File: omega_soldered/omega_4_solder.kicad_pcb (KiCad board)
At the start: 2 copper layers, 204.8 x 78 mm, 83 parts, among them J1 Conn_01x02_Female, U1 ProMicro

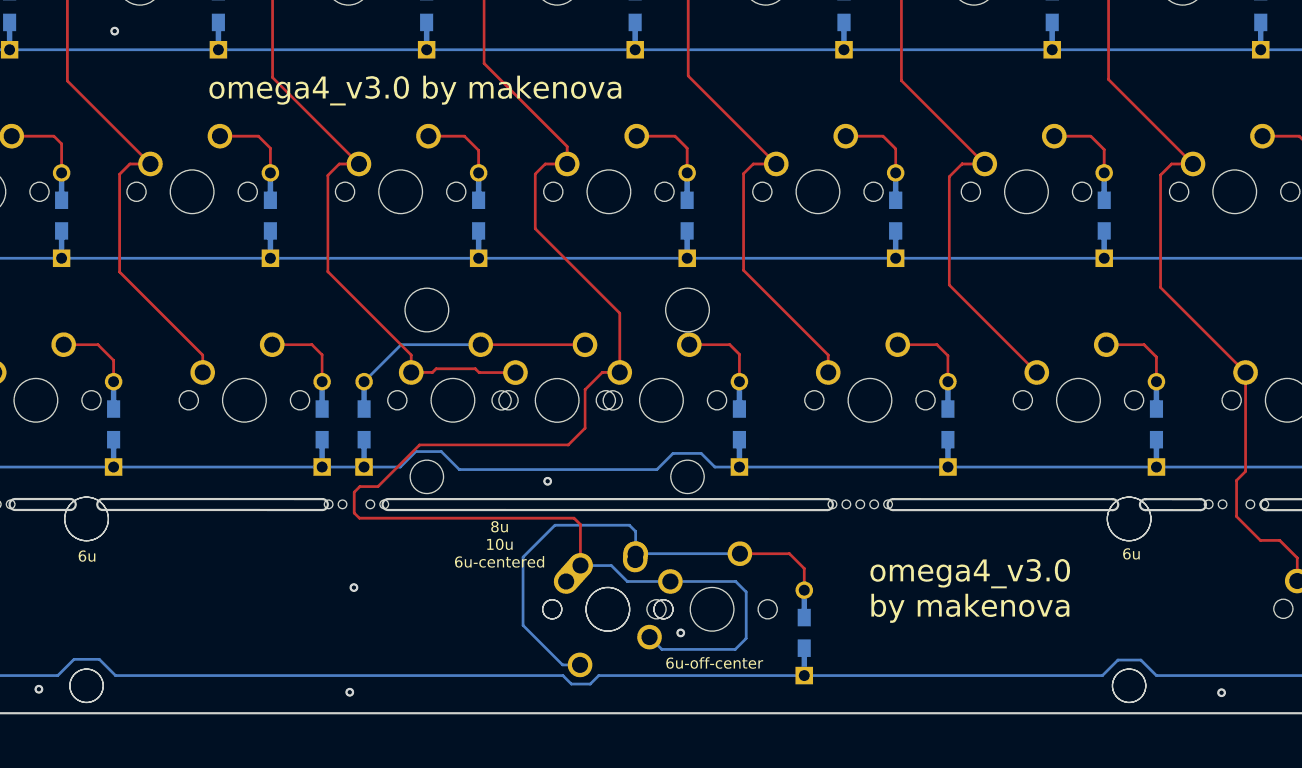
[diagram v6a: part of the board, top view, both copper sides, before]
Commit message: add split spacebar to breakaway row
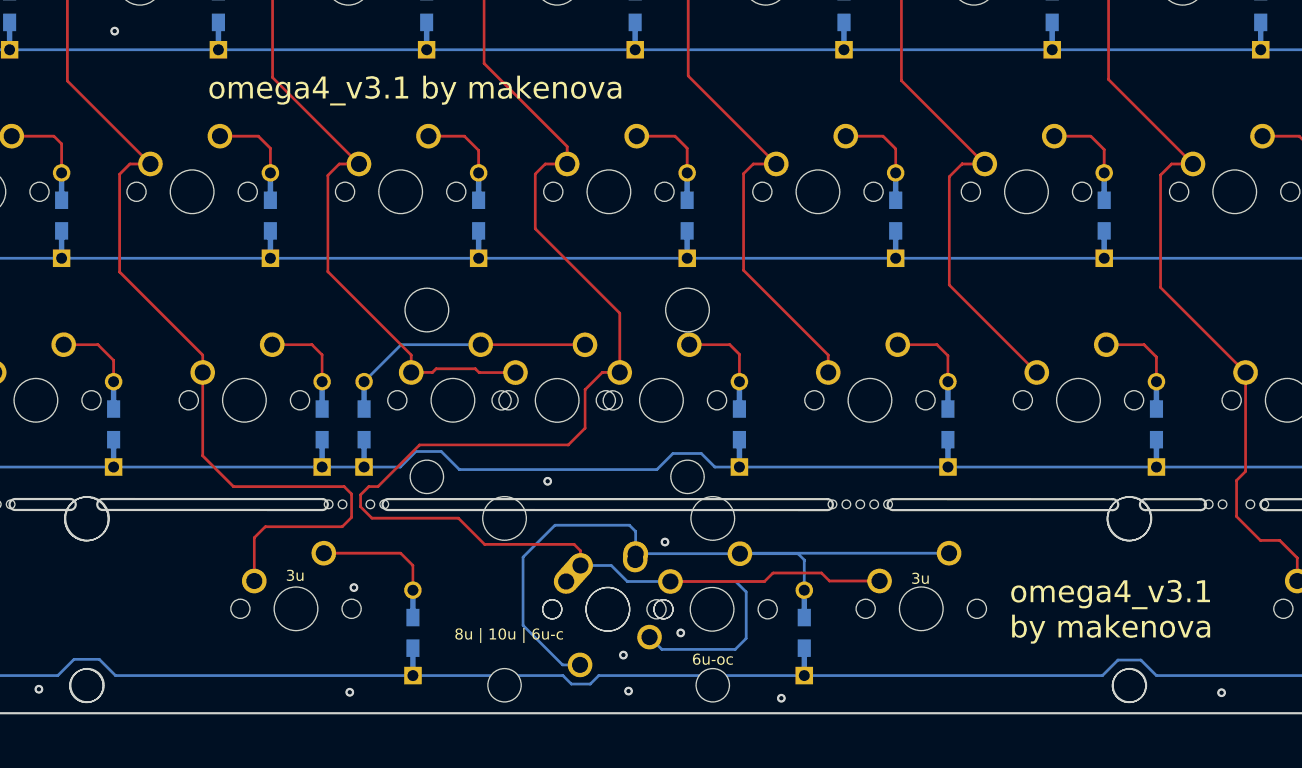
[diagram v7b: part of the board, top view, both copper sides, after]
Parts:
- added D36: D_Small, Keebio-Parts:Diode-Hybrid-Back, F.Cu at (140.4, 124.9)
- added MX39: MX-NoLED, MX_Only:MXOnly-3U-ReversedStabilizers-NoLED, F.Cu at (129.7, 122.7)
- added MX40: MX-NoLED, MX_Only:MXOnly-3U-ReversedStabilizers-NoLED, F.Cu at (186.8, 122.7)
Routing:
- net COL3: track 99.4 -> 137.8 mm
- net Net-(D33-Pad2): track 44.9 -> 64.6 mm
- net COL5: track 208.4 -> 225.1 mm
- net Net-(D36-Pad2): track 0.00 -> 10.9 mm
- net GND: vias 18 -> 22
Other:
- board text added: "3u"
- board text added: "6u-oc"
- board text added: "8u | 10u | 6u-c"
- board text added: "omega4_v3.1 by makenova"
- board text removed: "6u"
- board text removed: "6u-off-center"
- board text removed: "8u 10u 6u-centered"
- board text removed: "omega4_v3.0 by makenova"

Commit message: update readme images
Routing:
- net ROW3: track 237.6 -> 240.1 mm
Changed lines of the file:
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@@
   (segment (start 76.577741 109.802259) (end 76.577741 113.656741) (width 0.25) (layer "F.Cu") (net 34))
   (segment (start 75.20074 82.51285) (end 75.20074 95.26674) (width 0.25) (layer "F.Cu") (net 34))
-  (segment (start 111.716 127.3175) (end 113.1985 128.8) (width 0.25) (layer "B.Cu") (net 34))
+  (segment (start 226.025 127.5) (end 223.7185 127.5) (width 0.25) (layer "B.Cu") (net 34))
   (segment (start 93.025 127.45) (end 94.375 128.8) (width 0.25) (layer "B.Cu") (net 34))
   (segment (start 79.7 128.8) (end 89.15 128.8) (width 0.25) (layer "B.Cu") (net 34))
-  (segment (start 154.075 128.8) (end 154.85 129.575) (width 0.25) (layer "B.Cu") (net 34))
-  (segment (start 157.35 128.8) (end 203.3685 128.8) (width 0.25) (layer "B.Cu") (net 34))
-  (segment (start 226.025 127.5) (end 227.3 128.775) (width 0.25) (layer "B.Cu") (net 34))
-  (segment (start 204.7875 127.381) (end 206.883 127.381) (width 0.25) (layer "B.Cu") (net 34))
+  (segment (start 107.928 128.8) (end 98.75 128.8) (width 0.25) (layer "B.Cu") (net 34))
   (segment (start 89.15 128.8) (end 90.5 127.45) (width 0.25) (layer "B.Cu") (net 34))
-  (segment (start 227.3 128.775) (end 232.075 128.775) (width 0.25) (layer "B.Cu") (net 34))
+  (segment (start 171.4 128.8) (end 169.97 127.37) (width 0.25) (layer "B.Cu") (net 34))
+  (segment (start 203.3685 128.8) (end 171.4 128.8) (width 0.25) (layer "B.Cu") (net 34))
+  (segment (start 227.3 128.775) (end 226.025 127.5) (width 0.25) (layer "B.Cu") (net 34))
+  (segment (start 208.302 128.8) (end 206.883 127.381) (width 0.25) (layer "B.Cu") (net 34))
+  (segment (start 222.4185 128.8) (end 208.302 128.8) (width 0.25) (layer "B.Cu") (net 34))
+  (segment (start 166.07 127.37) (end 164.64 128.8) (width 0.25) (layer "B.Cu") (net 34))
+  (segment (start 232.075 128.775) (end 227.3 128.775) (width 0.25) (layer "B.Cu") (net 34))
+  (segment (start 223.7185 127.5) (end 222.4185 128.8) (width 0.25) (layer "B.Cu") (net 34))
+  (segment (start 157.35 128.8) (end 156.575 129.575) (width 0.25) (layer "B.Cu") (net 34))
   (segment (start 90.5 127.45) (end 93.025 127.45) (width 0.25) (layer "B.Cu") (net 34))
-  (segment (start 113.1985 128.8) (end 154.075 128.8) (width 0.25) (layer "B.Cu") (net 34))
-  (segment (start 156.575 129.575) (end 157.35 128.8) (width 0.25) (layer "B.Cu") (net 34))
-  (segment (start 107.928 128.8) (end 109.4105 127.3175) (width 0.25) (layer "B.Cu") (net 34))
-  (segment (start 98.75 128.8) (end 107.928 128.8) (width 0.25) (layer "B.Cu") (net 34))
-  (segment (start 206.883 127.381) (end 208.302 128.8) (width 0.25) (layer "B.Cu") (net 34))
+  (segment (start 145.52 128.8) (end 113.1985 128.8) (width 0.25) (layer "B.Cu") (net 34))
+  (segment (start 204.7875 127.381) (end 203.3685 128.8) (width 0.25) (layer "B.Cu") (net 34))
+  (segment (start 111.716 127.3175) (end 109.4105 127.3175) (width 0.25) (layer "B.Cu") (net 34))
+  (segment (start 113.1985 128.8) (end 111.716 127.3175) (width 0.25) (layer "B.Cu") (net 34))
   (segment (start 251.15 128.775) (end 232.075 128.775) (width 0.25) (layer "B.Cu") (net 34))
-  (segment (start 109.4105 127.3175) (end 111.716 127.3175) (width 0.25) (layer "B.Cu") (net 34))
-  (segment (start 222.4185 128.8) (end 223.7185 127.5) (width 0.25) (layer "B.Cu") (net 34))
+  (segment (start 156.575 129.575) (end 154.85 129.575) (width 0.25) (layer "B.Cu") (net 34))
+  (segment (start 154.075 128.8) (end 151.49 128.8) (width 0.25) (layer "B.Cu") (net 34))
+  (segment (start 151.49 128.8) (end 149.87 127.18) (width 0.25) (layer "B.Cu") (net 34))
+  (segment (start 149.87 127.18) (end 147.14 127.18) (width 0.25) (layer "B.Cu") (net 34))
+  (segment (start 154.85 129.575) (end 154.075 128.8) (width 0.25) (layer "B.Cu") (net 34))
   (segment (start 94.375 128.8) (end 98.75 128.8) (width 0.25) (layer "B.Cu") (net 34))
-  (segment (start 208.302 128.8) (end 222.4185 128.8) (width 0.25) (layer "B.Cu") (net 34))
-  (segment (start 154.85 129.575) (end 156.575 129.575) (width 0.25) (layer "B.Cu") (net 34))
-  (segment (start 223.7185 127.5) (end 226.025 127.5) (width 0.25) (layer "B.Cu") (net 34))
-  (segment (start 203.3685 128.8) (end 204.7875 127.381) (width 0.25) (layer "B.Cu") (net 34))
+  (segment (start 147.14 127.18) (end 145.52 128.8) (width 0.25) (layer "B.Cu") (net 34))
+  (segment (start 109.4105 127.3175) (end 107.928 128.8) (width 0.25) (layer "B.Cu") (net 34))
+  (segment (start 206.883 127.381) (end 204.7875 127.381) (width 0.25) (layer "B.Cu") (net 34))
+  (segment (start 164.64 128.8) (end 157.35 128.8) (width 0.25) (layer "B.Cu") (net 34))
+  (segment (start 169.97 127.37) (end 166.07 127.37) (width 0.25) (layer "B.Cu") (net 34))
   (segment (start 75.14 117.62) (end 78.495 117.62) (width 0.25) (layer "F.Cu") (net 35))
   (segment (start 79.7 118.825) (end 78.495 117.62) (width 0.25) (layer "F.Cu") (net 35))
@@
   (segment (start 94.165 117.62) (end 97.47 117.62) (width 0.25) (layer "F.Cu") (net 36))
   (segment (start 98.75 121) (end 98.75 118.9) (width 0.25) (layer "F.Cu") (net 36))
-  (segment (start 170.289 117.62) (end 170.2435 117.6655) (width 0.25) (layer "F.Cu") (net 37))
   (segment (start 160.7185 115.6335) (end 160.7185 117.6655) (width 0.25) (layer "B.Cu") (net 37))
-  (segment (start 161.2585 117.6655) (end 170.2435 117.6655) (width 0.25) (layer "B.Cu") (net 37))
   (segment (start 153.3525 115.062) (end 160.147 115.062) (width 0.25) (layer "B.Cu") (net 37))
-  (segment (start 175.5555 117.6655) (end 176.15 118.26) (width 0.25) (layer "B.Cu") (net 37))
+  (segment (start 170.2435 117.6655) (end 160.7185 117.6655) (width 0.25) (layer "B.Cu") (net 37))
   (segment (start 160.147 115.062) (end 160.7185 115.6335) (width 0.25) (layer "B.Cu") (net 37))
-  (segment (start 176.125 118.285) (end 176.125 121) (width 0.25) (layer "B.Cu") (net 37))
-  (segment (start 170.2435 117.6655) (end 175.5555 117.6655) (width 0.25) (layer "B.Cu") (net 37))
+  (segment (start 170.289 117.62) (end 170.2435 117.6655) (width 0.25) (layer "B.Cu") (net 37))
+  (segment (start 176.125 118.955) (end 176.125 121) (width 0.25) (layer "B.Cu") (net 37))
   (segment (start 150.4315 117.983) (end 153.3525 115.062) (width 0.25) (layer "B.Cu") (net 37))
+  (segment (start 170.2435 117.6655) (end 174.8355 117.6655) (width 0.25) (layer "B.Cu") (net 37))
+  (segment (start 155.6385 127.8255) (end 154.04751 127.8255) (width 0.25) (layer "B.Cu") (net 37))
   (segment (start 189.354774 117.62) (end 170.289 117.62) (width 0.25) (layer "B.Cu") (net 37))
-  (segment (start 155.6385 127.8255) (end 154.04751 127.8255) (width 0.25) (layer "B.Cu") (net 37))
   (segment (start 160.6785 118.2455) (end 161.2585 117.6655) (width 0.25) (layer "B.Cu") (net 37))
   (segment (start 154.04751 127.8255) (end 150.4315 124.20949) (width 0.25) (layer "B.Cu") (net 37))
-  (segment (start 170.289 117.62) (end 170.2435 117.6655) (width 0.25) (layer "B.Cu") (net 37))
+  (segment (start 174.8355 117.6655) (end 176.125 118.955) (width 0.25) (layer "B.Cu") (net 37))
   (segment (start 150.4315 124.20949) (end 150.4315 117.983) (width 0.25) (layer "B.Cu") (net 37))
-  (segment (start 176.15 118.26) (end 176.125 118.285) (width 0.25) (layer "B.Cu") (net 37))
   (segment (start 232.075 118.5) (end 232.075 120.975) (width 0.25) (layer "F.Cu") (net 38))
   (segment (start 231.195 117.62) (end 232.075 118.5) (width 0.25) (layer "F.Cu") (net 38))
